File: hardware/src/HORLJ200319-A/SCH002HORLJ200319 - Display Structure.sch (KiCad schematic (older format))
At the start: 12 parts

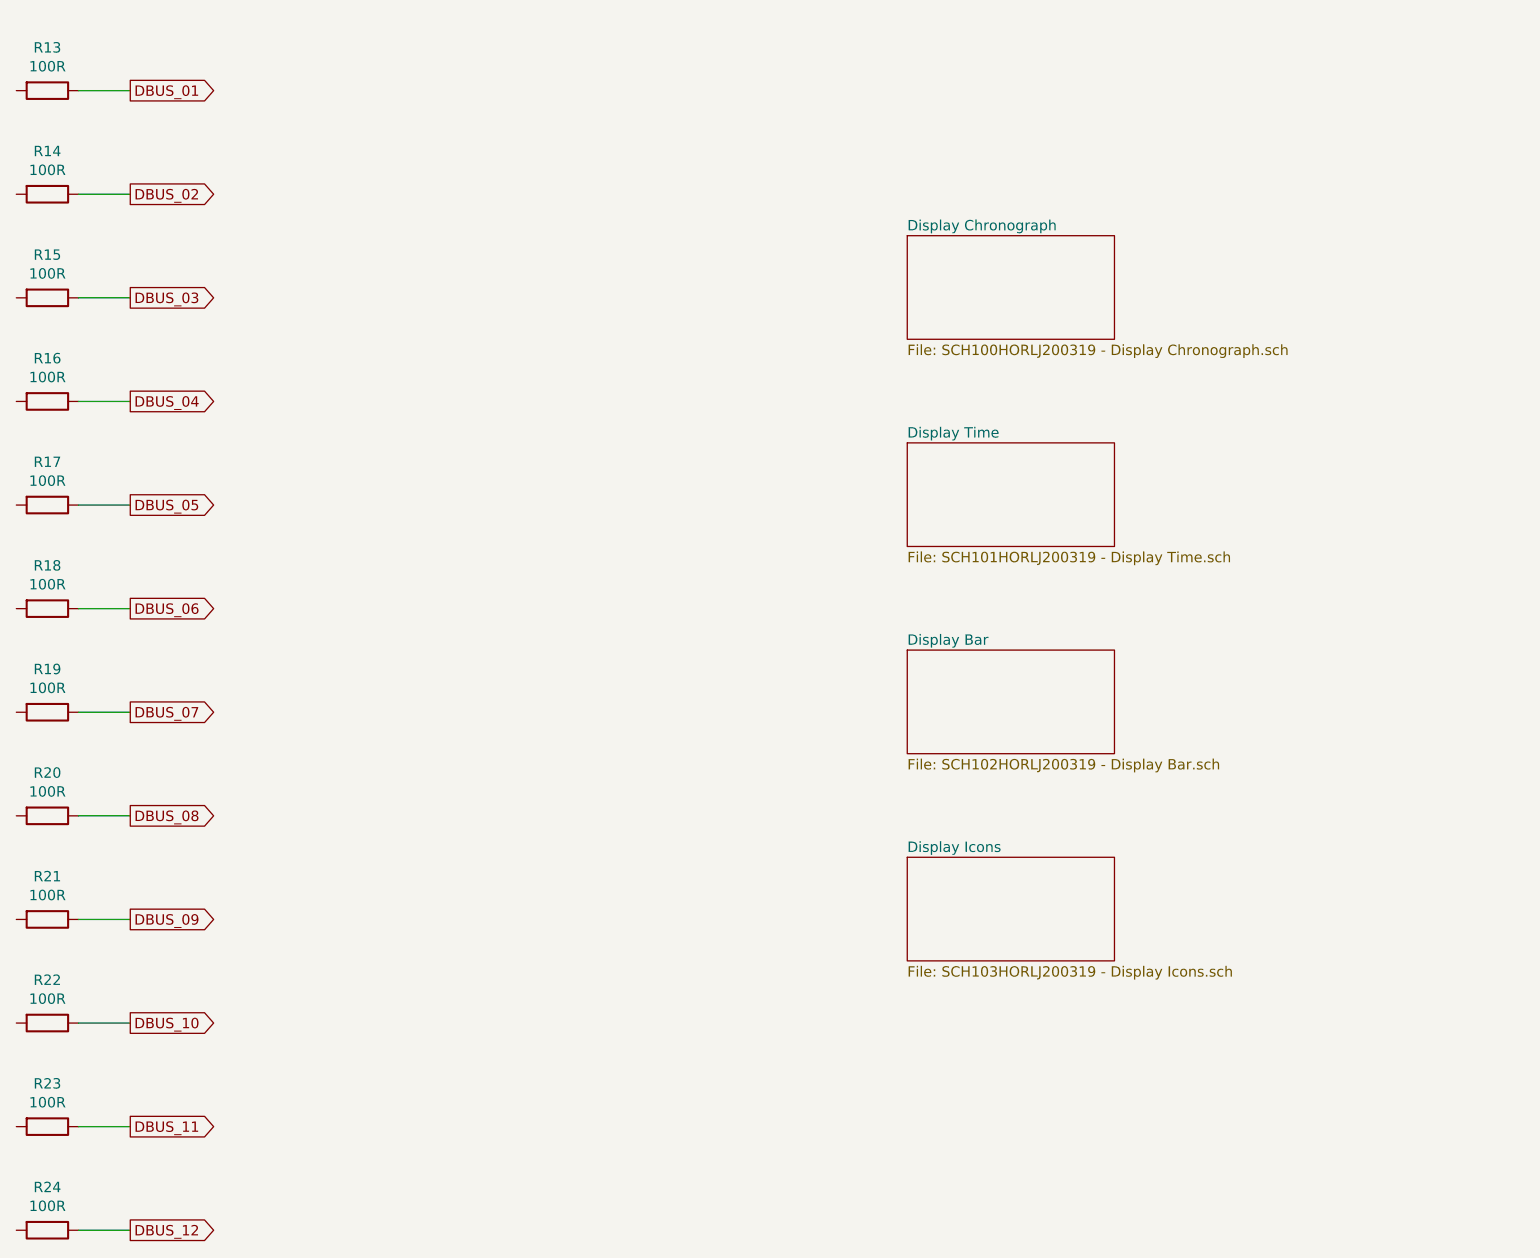
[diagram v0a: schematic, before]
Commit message: Insere MockUps digitais e inicia o projeto da PCB.
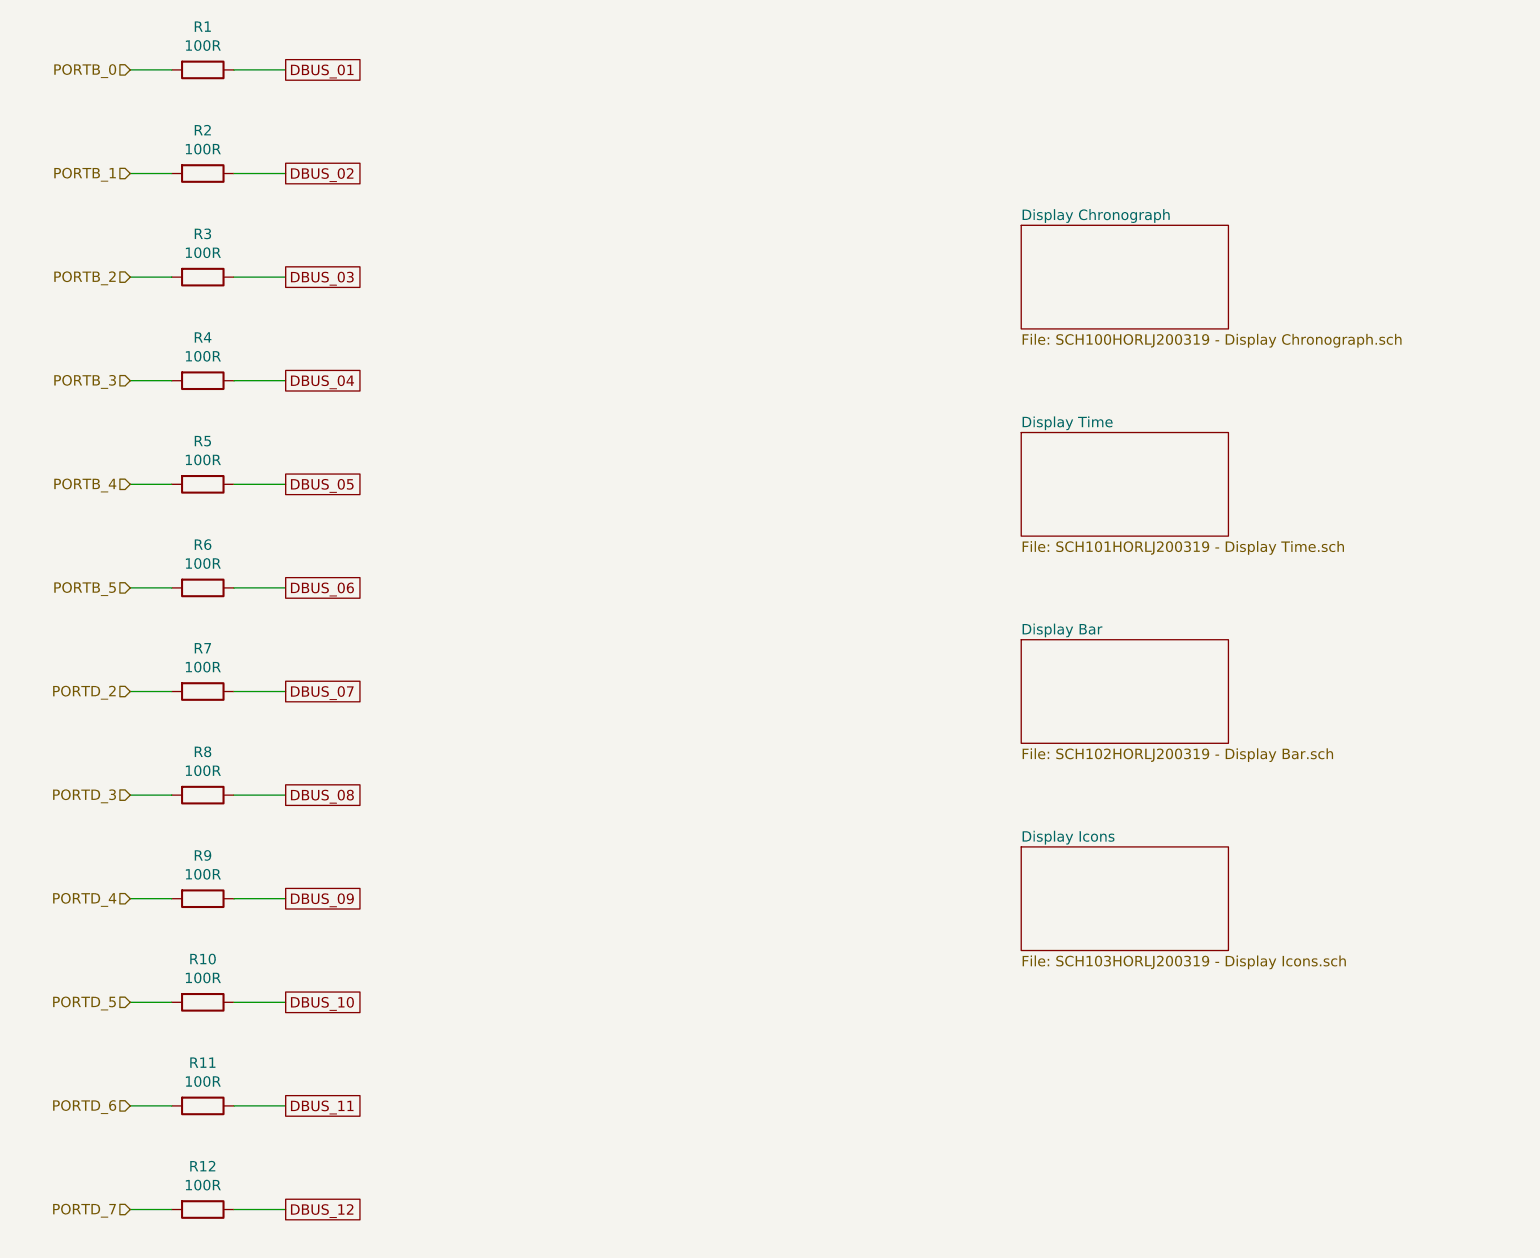
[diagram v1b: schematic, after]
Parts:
- renumbered R13 to R1, R22 to R10, R23 to R11, R24 to R12, R14 to R2, R15 to R3, R16 to R4, R17 to R5, R18 to R6, R19 to R7, R20 to R8, R21 to R9
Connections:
- net PORTB_1: now reaches R2.2
- net PORTD_7: now reaches R12.2
- net PORTD_6: now reaches R11.2
- net PORTD_5: now reaches R10.2
- net PORTD_4: now reaches R9.2
- net PORTD_3: now reaches R8.2
- net PORTD_2: now reaches R7.2
- net PORTB_5: now reaches R6.2
- net PORTB_4: now reaches R5.2
- net PORTB_3: now reaches R4.2
- net PORTB_2: now reaches R3.2
- net PORTB_0: now reaches R1.2
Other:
- moved on the sheet: R1, R10, R11, R12, R2, R3, R4, R5, R6, R7, R8, R9
